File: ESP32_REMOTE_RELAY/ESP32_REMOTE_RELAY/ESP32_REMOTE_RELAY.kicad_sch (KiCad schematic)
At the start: 15 parts, among them J1 AC_MAINS, J2 Bulvack LM2596, J3 RC Snubber Mod., J4 RC Snubber Mod., J5 Bulvack LM2596, J6 Bulvack LM2596, J7 Bulvack LM2596, K1 Teylen Robot Optocoupler 3V3 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, K2 Teylen Robot Optocoupler 3V3 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, U1 ESP32-WROOM-32

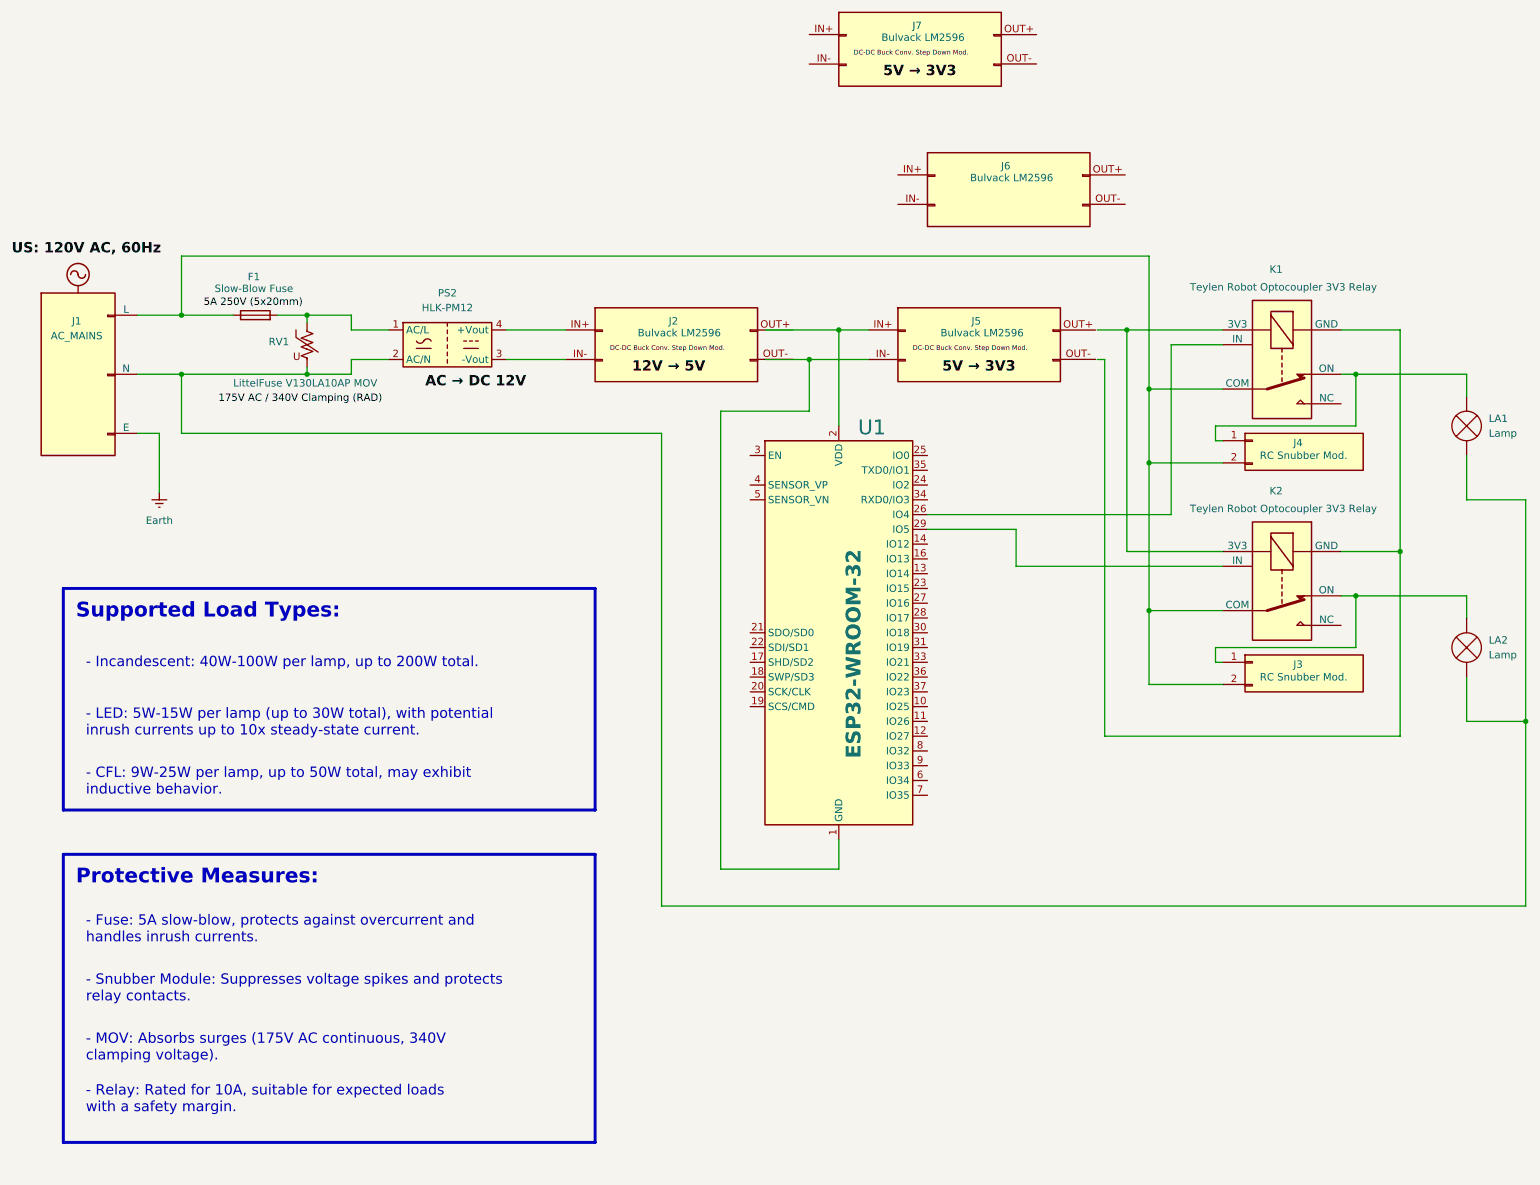
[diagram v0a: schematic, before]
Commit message: 3V3 relays were DOA, so switched to HLK-PM12, 12V->3V3 Buck, and 12V Relay with 3V3 trigger
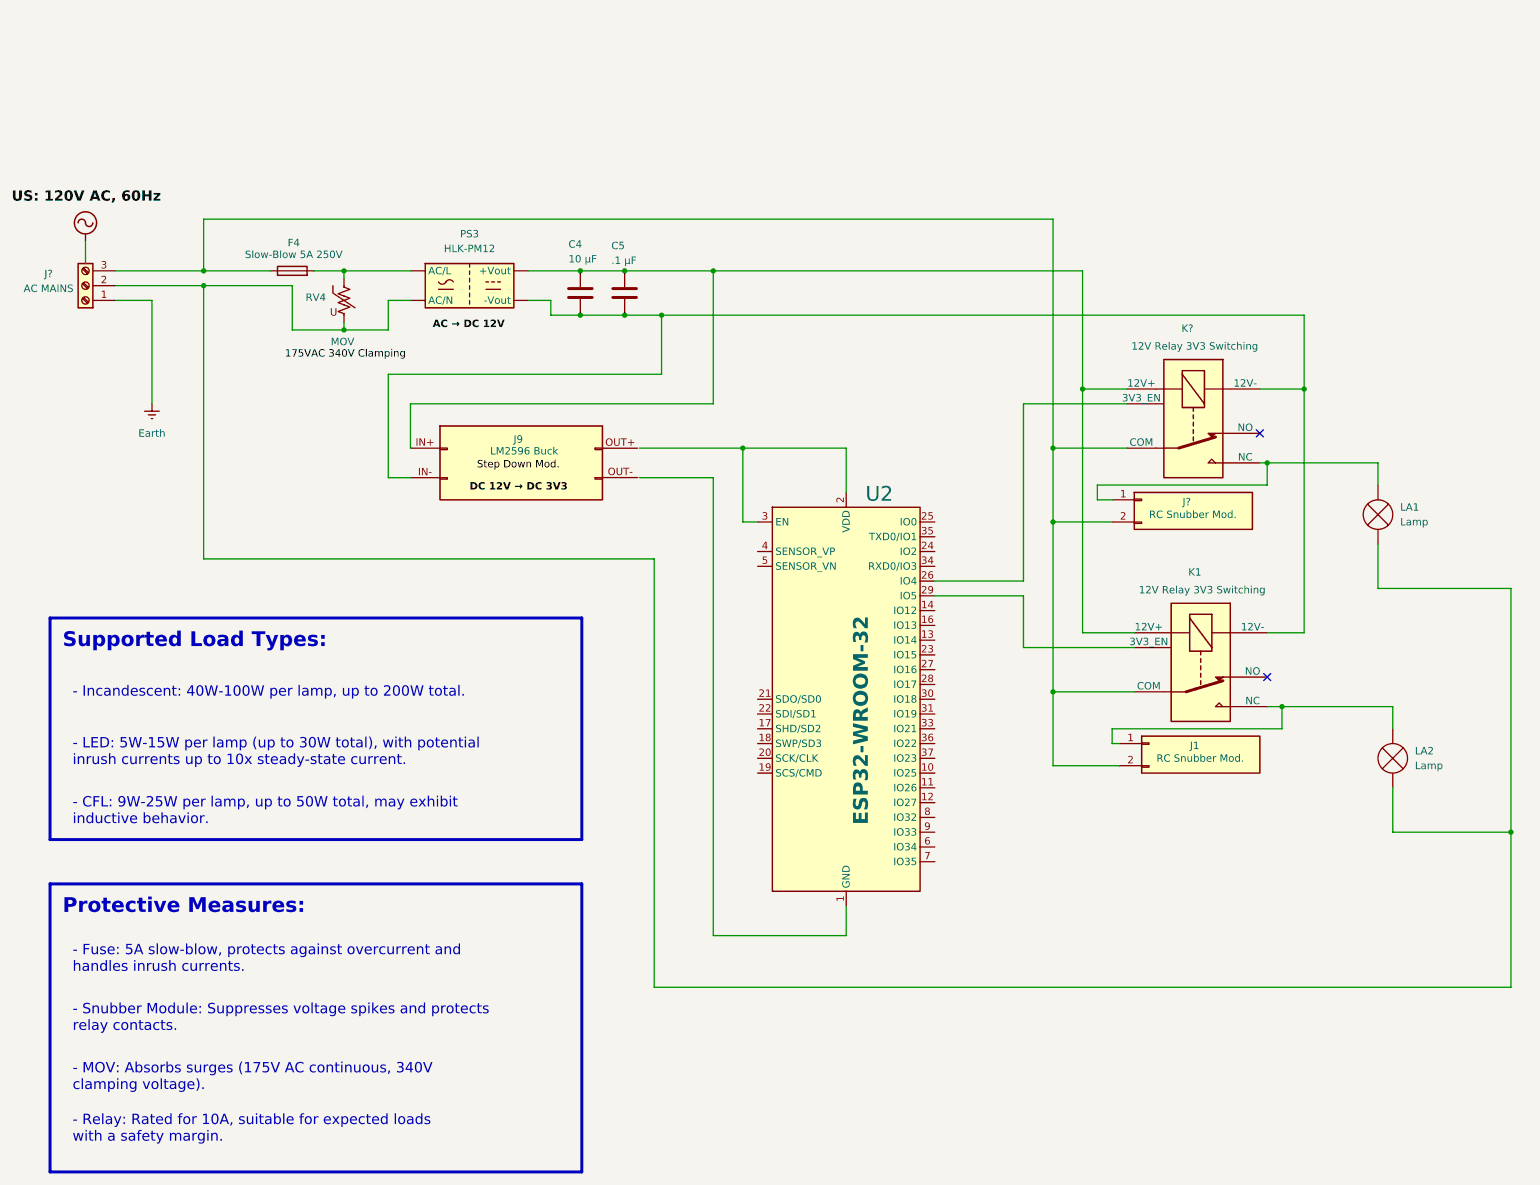
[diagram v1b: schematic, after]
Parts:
- removed F1: Slow-Blow Fuse, symbol Device:Fuse
- removed J1: AC_MAINS, symbol Connector_Generic:Conn_01x03
- removed J2, J5, J6, J7: Bulvack LM2596, symbol Connector_Generic:Conn_02x02_Counter_Clockwise
- removed J3, J4: RC Snubber Mod., symbol Connector_Generic:Conn_01x02
- removed K2: Teylen Robot Optocoupler 3V3 Relay, Relay_THT:Relay_SPDT_StandexMeder_SIL_Form1C, symbol Relay:SILxx-1Cxx-51x
- removed PS2: HLK-PM12, Converter_ACDC:Converter_ACDC_Hi-Link_HLK-PMxx, symbol Converter_ACDC:HLK-PM12
- removed RV1: LittelFuse V130LA10AP MOV, symbol Device:Varistor_US
- removed U1: ESP32-WROOM-32, RF_Module:ESP32-WROOM-32, symbol RF_Module:ESP32-WROOM-32
- added C4: 10 µF, symbol Device:C
- added C5: .1 µF, symbol Device:C
- added F4: Slow-Blow 5A 250V, symbol Device:Fuse
- added J1, J?: RC Snubber Mod., symbol Connector_Generic:Conn_01x02
- added J9: LM2596 Buck, symbol Connector_Generic:Conn_02x02_Counter_Clockwise
- added J?: AC MAINS, symbol Connector:Screw_Terminal_01x03
- added K?: 12V Relay 3V3 Switching, Relay_THT:Relay_SPDT_StandexMeder_SIL_Form1C, symbol Relay:SILxx-1Cxx-51x
- added PS3: HLK-PM12, Converter_ACDC:Converter_ACDC_Hi-Link_HLK-PMxx, symbol Converter_ACDC:HLK-PM03
- added RV4: MOV, symbol Device:Varistor_US
- added U2: ESP32-WROOM-32, RF_Module:ESP32-WROOM-32, symbol RF_Module:ESP32-WROOM-32
- K1: value Teylen Robot Optocoupler 3V3 Relay -> 12V Relay 3V3 Switching
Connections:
- net Earth: now also J?.1 (Pin_1)
- net at LA2.2 (+): now also K1.1 (NC), J1.1 (Pin_1)
- net at K1.3 (12V+): now also C4.1, C5.1, J9.IN+ (Pin_1), K?.3 (12V+), PS3.4 (+Vout)
- net at K1.5 (12V-): now also C4.2, C5.2, J9.IN- (Pin_2), K?.5 (12V-), PS3.3 (-Vout)
- net at K1.7 (COM): now also F4.1, J1.2 (Pin_2), J?.2 (Pin_2), J?.3 (Pin_3), K?.7 (COM)
- net at LA1.1 (-), LA2.1 (-): now also J?.2 (Pin_2), PS3.2 (AC/N), RV4.2
- net at K1.2 (NO): no longer LA1.2 (+)
- net at K1.4 (3V3_EN): now also U2.29 (IO5)
- new net: J?.1 (Pin_1), K?.1 (NC), LA1.2 (+)
- new net: K?.4 (3V3_EN), U2.26 (IO4)
- new net: F4.2, PS3.1 (AC/L), RV4.1
- new net: U2.1 (GND), U2.15 (GND), U2.38 (GND), U2.39 (GND)
- new net: U2.2 (VDD), U2.3 (EN)
- no-connect marks 0 -> 2
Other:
- title: ESP32 Remote Relay Circuit -> (none)
